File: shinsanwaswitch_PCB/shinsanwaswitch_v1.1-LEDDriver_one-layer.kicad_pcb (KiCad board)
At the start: 2 copper layers, 26.3 x 15.4 mm, 9 parts, among them J1 Conn_01x05_Male, Q1 2SC5395

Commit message: Update for DIY-make boards
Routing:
- net (no net): vias 0 -> 5
- added copper zone on B.Cu, net (none)
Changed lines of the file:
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@@
     (effects (font (size 0.5 0.5) (thickness 0.125)))
   )
+  (via (at 137.525 88.7) (size 2.05) (drill 1.98) (layers "F.Cu" "B.Cu") (free) (net 0))
+  (via (at 146.1 76.8) (size 2.65) (drill 2.58) (layers "F.Cu" "B.Cu") (free) (net 0))
+  (via (at 149.78 86.2) (size 1.1) (drill 1) (layers "F.Cu" "B.Cu") (free) (net 0))
+  (via (at 151.1 76.79) (size 2.65) (drill 2.58) (layers "F.Cu" "B.Cu") (free) (net 0))
+  (via (at 149.78 88.7) (size 1.5) (drill 1.4) (layers "F.Cu" "B.Cu") (free) (net 0))
   (segment (start 151.145 87.325) (end 148.395 87.325) (width 0.7) (layer "B.Cu") (net 1))
   (segment (start 148.395 87.325) (end 147.27 86.2) (width 0.7) (layer "B.Cu") (net 1))
@@
   (segment (start 145.265299 83.541846) (end 147.298694 83.541846) (width 0.8) (layer "B.Cu") (net 8))
   (segment (start 137.47 83.72) (end 133.62 83.72) (width 0.8) (layer "B.Cu") (net 8))
+  (zone (net 0) (net_name "") (layer "B.Cu") (hatch edge 0.508)
+    (connect_pads (clearance 0.508))
+    (min_thickness 0.254) (filled_areas_thickness no)
+    (fill yes (thermal_gap 0.508) (thermal_bridge_width 0.508))
+    (polygon
+      (pts
+        (xy 155.194 90.678)
+        (xy 127 90.678)
+        (xy 127 74.168)
+        (xy 155.194 74.168)
+      )
+    )
+  )
 )

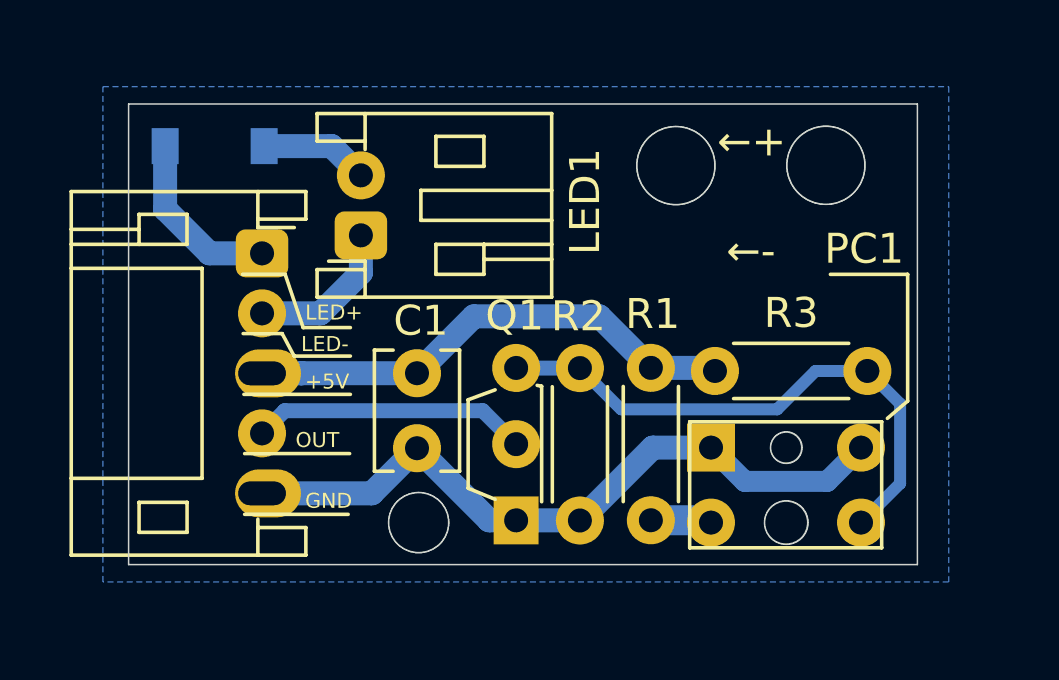
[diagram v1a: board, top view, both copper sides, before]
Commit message: Massive update of DIY-boards to make it easier to print and drill
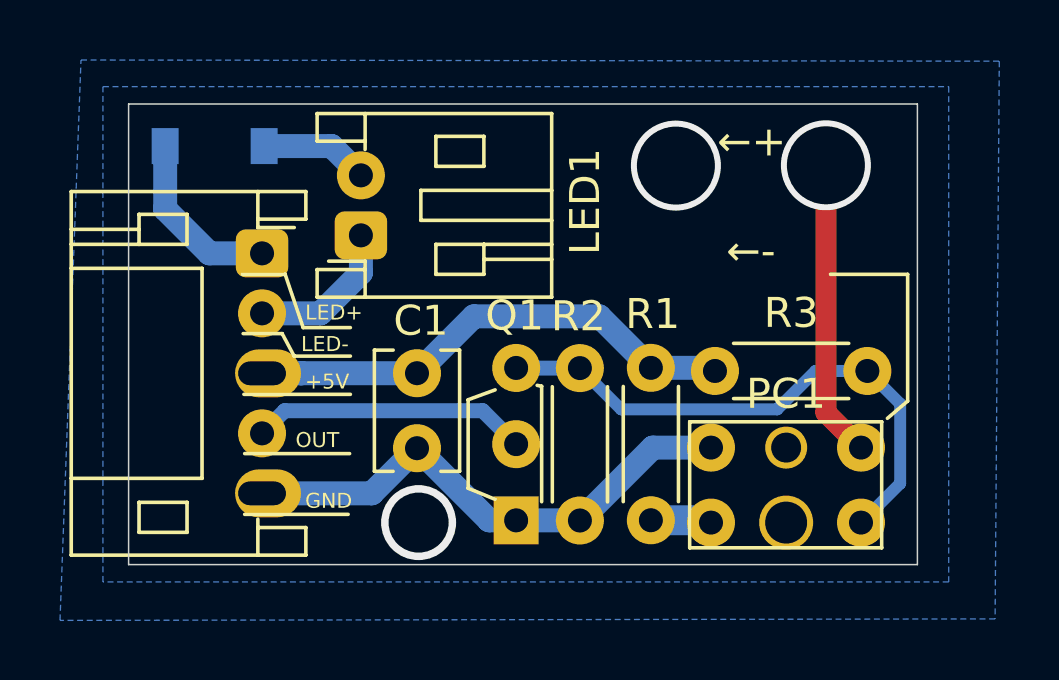
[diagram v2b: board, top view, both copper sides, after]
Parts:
- PC1: footprint RPI-221:RPI-352 -> RPI-221:RPI-352_otherholes
- moved PC1 4.74 mm to (149.8, 86.2)
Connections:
- PC1 pad : (no net) -> GND
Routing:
- net GND: track 23.5 -> 27.5 mm, vias 0 -> 3
- net (no net): vias 5 -> 0
- added copper zone on B.Cu, net GND
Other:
- outline, holes or cut-outs redrawn
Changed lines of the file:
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@@
-(kicad_pcb (version 20210722) (generator pcbnew)
+(kicad_pcb (version 20210824) (generator pcbnew)
   (general
     (thickness 1)
@@
     )
     (pad_to_mask_clearance 0)
+    (grid_origin 0.01 0.01)
     (pcbplotparams
       (layerselection 0x003ffff_ffffffff)
@@
     )
   )
-  (footprint "RPI-221:RPI-352" (layer "F.Cu")
-    (at 146.5 89.6)
-    (property "Sheetfile" "shinsanwaswitch_v1.1-LEDDriver_one-layer.kicad_sch")
-    (property "Sheetname" "")
-    (attr through_hole)
-    (fp_text reference "PC1" (at 5.875 -10.025 unlocked) (layer "F.SilkS")
-      (effects (font (size 1 1) (thickness 0.15)))
-    )
-    (fp_text value "RPI-352" (at 3.21 -2.2 unlocked) (layer "F.Fab")
-      (effects (font (size 0.5 0.5) (thickness 0.125)))
-    )
-    (fp_line (start 0.06 -4.26) (end 6.46 -4.26) (layer "F.SilkS") (width 0.12))
-    (fp_line (start 6.46 -0.06) (end 0.06 -0.06) (layer "F.SilkS") (width 0.12))
-    (fp_line (start 6.46 -4.26) (end 6.46 -0.06) (layer "F.SilkS") (width 0.12))
-    (fp_line (start 0.06 -0.06) (end 0.06 -4.26) (layer "F.SilkS") (width 0.12))
-    (pad "" np_thru_hole circle locked (at 3.275 -3.4) (size 1.03 1.03) (drill 1.03) (layers *.Mask))
-    (pad "" np_thru_hole circle locked (at 3.275 -0.9) (size 1.43 1.43) (drill 1.43) (layers *.Mask))
-    (pad "1" thru_hole rect locked (at 0.77 -3.4) (size 1.6 1.6) (drill oval 0.8) (layers *.Cu *.Mask)
+  (footprint "RPI-221:RPI-352_otherholes" (layer "F.Cu")
+    (at 149.775 86.18)
+    (property "Sheetfile" "shinsanwaswitch_v1.1-LEDDriver_one-layer.kicad_sch")
+    (property "Sheetname" "")
+    (attr through_hole)
+    (fp_text reference "PC1" (at -0.005 -1.77 unlocked) (layer "F.SilkS")
+      (effects (font (size 1 1) (thickness 0.15)))
+    )
+    (fp_text value "RPI-352" (at -0.065 -3.37 unlocked) (layer "F.Fab")
+      (effects (font (size 1 1) (thickness 0.15)))
+    )
+    (fp_line (start 3.185 3.36) (end -3.215 3.36) (layer "F.SilkS") (width 0.12))
+    (fp_line (start -3.215 3.36) (end -3.215 -0.84) (layer "F.SilkS") (width 0.12))
+    (fp_line (start 3.185 -0.84) (end 3.185 3.36) (layer "F.SilkS") (width 0.12))
+    (fp_line (start -3.215 -0.84) (end 3.185 -0.84) (layer "F.SilkS") (width 0.12))
+    (pad "" thru_hole circle (at 0 2.52) (size 1.8 1.8) (drill 1.4) (layers *.Cu *.Mask)
+      (net 1 "GND"))
+    (pad "" thru_hole circle (at 0 0.02) (size 1.4 1.4) (drill 1) (layers *.Cu *.Mask)
+      (net 1 "GND"))
+    (pad "1" thru_hole circle locked (at -2.505 0.02) (size 1.6 1.6) (drill 0.8) (layers *.Cu *.Mask)
       (net 1 "GND") (pintype "passive"))
-    (pad "2" thru_hole circle locked (at 0.77 -0.9) (size 1.6 1.6) (drill oval 0.8) (layers *.Cu *.Mask)
+    (pad "2" thru_hole circle locked (at -2.505 2.52) (size 1.6 1.6) (drill 0.8) (layers *.Cu *.Mask)
       (net 3 "Net-(PC1-Pad2)") (pintype "passive"))
-    (pad "3" thru_hole circle locked (at 5.77 -0.9) (size 1.6 1.6) (drill oval 0.8) (layers *.Cu *.Mask)
+    (pad "3" thru_hole circle locked (at 2.495 2.52) (size 1.6 1.6) (drill 0.8) (layers *.Cu *.Mask)
       (net 4 "Net-(PC1-Pad3)") (pintype "passive"))
-    (pad "4" thru_hole circle locked (at 5.77 -3.4) (size 1.6 1.6) (drill oval 0.8) (layers *.Cu *.Mask)
+    (pad "4" thru_hole circle locked (at 2.495 0.02) (size 1.6 1.6) (drill 0.8) (layers *.Cu *.Mask)
       (net 1 "GND") (pintype "passive"))
-    (model "${KIPRJMOD}/rpi-352.STEP"
-      (offset (xyz 3.2 10.65 2.7))
-      (scale (xyz 1 1 1))
-      (rotate (xyz -90 0 0))
-    )
   )
   (footprint "Resistor_THT:R_Axial_DIN0204_L3.6mm_D1.6mm_P5.08mm_Horizontal" (layer "F.Cu")
@@
   (gr_line (start 153.15 85.225) (end 153.825 84.65) (layer "F.SilkS") (width 0.12))
   (gr_rect (start 127.85651 74.746407) (end 154.15 90.1) (layer "Edge.Cuts") (width 0.05) (fill none))
-  (gr_circle (center 146.1 76.8) (end 147.4 76.8) (layer "Edge.Cuts") (width 0.05) (fill none))
-  (gr_circle (center 151.1 76.79) (end 152.4 76.79) (layer "Edge.Cuts") (width 0.05) (fill none))
-  (gr_circle (center 137.525 88.7) (end 138.525 88.7) (layer "Edge.Cuts") (width 0.05) (fill none))
   (gr_text "GND" (at 130.275 87.7) (layer "B.SilkS")
     (effects (font (size 0.5 0.5) (thickness 0.125)) (justify mirror))
@@
     (effects (font (size 0.5 0.5) (thickness 0.125)))
   )
-  (via (at 137.525 88.7) (size 2.05) (drill 1.98) (layers "F.Cu" "B.Cu") (free) (net 0))
-  (via (at 146.1 76.8) (size 2.65) (drill 2.58) (layers "F.Cu" "B.Cu") (free) (net 0))
-  (via (at 149.78 86.2) (size 1.1) (drill 1) (layers "F.Cu" "B.Cu") (free) (net 0))
-  (via (at 151.1 76.79) (size 2.65) (drill 2.58) (layers "F.Cu" "B.Cu") (free) (net 0))
-  (via (at 149.78 88.7) (size 1.5) (drill 1.4) (layers "F.Cu" "B.Cu") (free) (net 0))
-  (segment (start 151.145 87.325) (end 148.395 87.325) (width 0.7) (layer "B.Cu") (net 1))
-  (segment (start 148.395 87.325) (end 147.27 86.2) (width 0.7) (layer "B.Cu") (net 1))
+  (segment (start 151.1 85.03) (end 151.1 76.79) (width 0.7) (layer "F.Cu") (net 1))
+  (segment (start 152.27 86.2) (end 151.1 85.03) (width 0.7) (layer "F.Cu") (net 1))
+  (via (at 151.1 76.79) (size 3) (drill 2.6) (layers "F.Cu" "B.Cu") (free) (net 1))
+  (via (at 137.524 88.7) (size 2.5) (drill 2) (layers "F.Cu" "B.Cu") (free) (net 1))
+  (via (at 146.1 76.8) (size 3) (drill 2.6) (layers "F.Cu" "B.Cu") (free) (net 1))
   (segment (start 140.775 88.625) (end 139.875 88.625) (width 0.8) (layer "B.Cu") (net 1))
   (segment (start 142.9 88.63) (end 145.33 86.2) (width 0.8) (layer "B.Cu") (net 1))
@@
   (segment (start 145.33 86.2) (end 147.27 86.2) (width 0.8) (layer "B.Cu") (net 1))
   (segment (start 132.304628 87.725) (end 135.965 87.725) (width 0.8) (layer "B.Cu") (net 1))
-  (segment (start 152.27 86.2) (end 151.145 87.325) (width 0.7) (layer "B.Cu") (net 1))
   (segment (start 142.895 88.625) (end 142.9 88.63) (width 0.7) (layer "B.Cu") (net 1))
   (segment (start 134.625 76.15) (end 135.6 77.125) (width 0.8) (layer "B.Cu") (net 2))
@@
   (segment (start 145.265299 83.541846) (end 147.298694 83.541846) (width 0.8) (layer "B.Cu") (net 8))
   (segment (start 137.47 83.72) (end 133.62 83.72) (width 0.8) (layer "B.Cu") (net 8))
-  (zone (net 0) (net_name "") (layer "B.Cu") (hatch edge 0.508)
-    (connect_pads (clearance 0.508))
+  (zone (net 1) (net_name "GND") (layer "B.Cu") (hatch edge 0.508)
+    (connect_pads yes (clearance 0.508))
     (min_thickness 0.254) (filled_areas_thickness no)
     (fill yes (thermal_gap 0.508) (thermal_bridge_width 0.508))
@@
       )
     )
+  )
+  (zone (net 0) (net_name "") (layer "B.Cu") (hatch edge 0.508)
+    (connect_pads (clearance 0.508))
+    (min_thickness 0.254) (filled_areas_thickness no)
+    (fill yes (thermal_gap 0.508) (thermal_bridge_width 0.508))
+    (polygon
+      (pts
+        (xy 156.88 73.32)
+        (xy 156.74 91.91)
+        (xy 125.57 91.96)
+        (xy 126.27 73.28)
+      )
+    )
